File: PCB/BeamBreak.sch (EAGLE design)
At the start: 8 parts, among them J1 AUDIO-CONNECTOR-6P-SMD-344003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, Q1 MOSFET-N-0440200P1

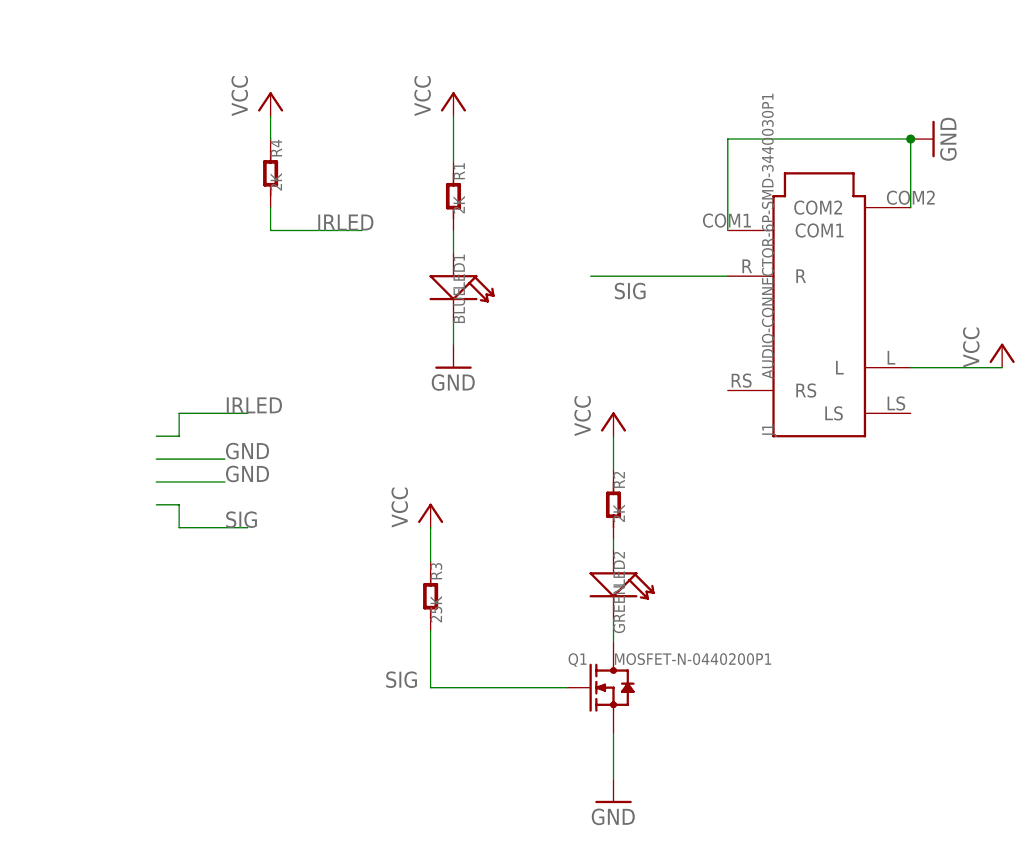
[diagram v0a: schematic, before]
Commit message: Changed connections for wires to a header so that solder mask will be properly applied.
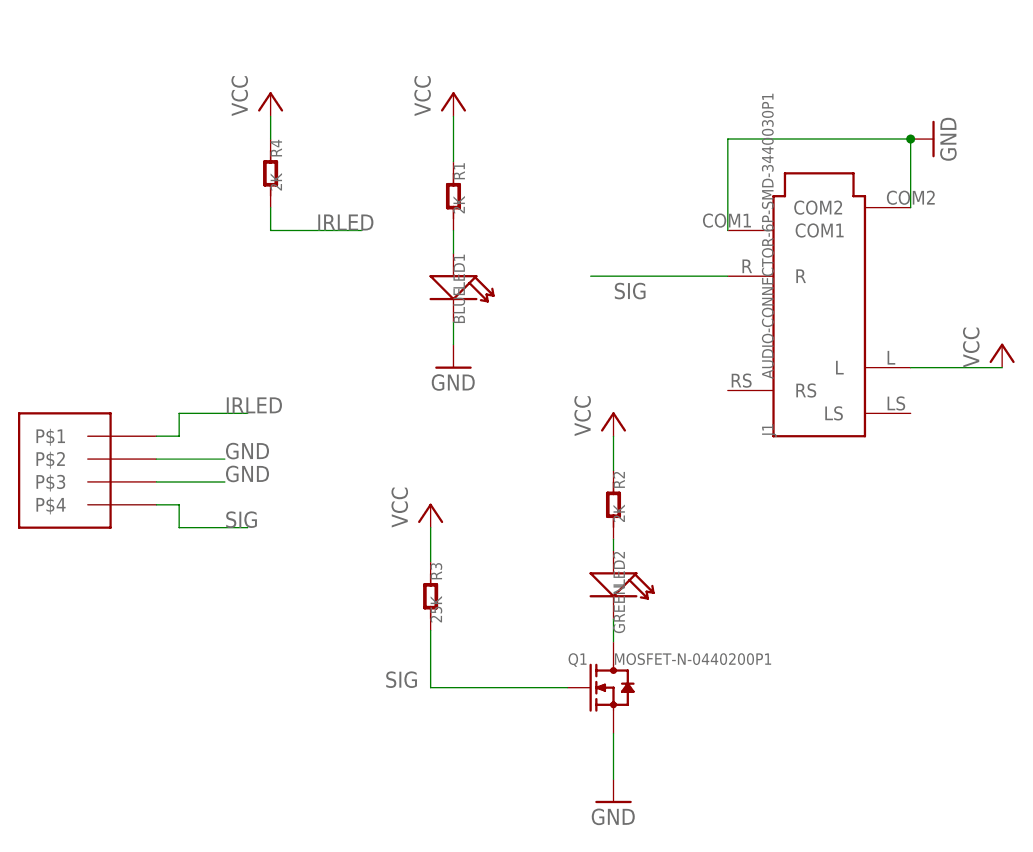
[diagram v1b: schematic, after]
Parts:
- added U$1: HO4, BeamBreak:HO4
- J1: device OPL:AUDIO-CONNECTOR-6P-SMD-3440030P1 -> BeamBreak:AUDIO-CONNECTOR-6P-SMD-3440030P1
- LED1, LED2: device OPL:LED -> BeamBreak:LED
- Q1: device OPL:MOSFET-N-0440200P1 -> BeamBreak:MOSFET-N-0440200P1
- R1, R2, R3: device OPL:R-0603 -> BeamBreak:R-0603
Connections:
- net GND: now also U$1.P$2, U$1.P$3
- net IRLED: now also U$1.P$1
- net SIG: now also U$1.P$4
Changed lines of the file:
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@@
 </classes>
 <parts>
-<part name="R3" library="OPL" deviceset="R*" device="-0603" value="25K"/>
+<part name="R3" library="BeamBreak" deviceset="R*" device="-0603" value="25K"/>
 <part name="GND2" library="SparkFun" deviceset="GND" device=""/>
 <part name="P+3" library="supply1" deviceset="VCC" device=""/>
 <part name="P+4" library="supply1" deviceset="VCC" device=""/>
-<part name="R2" library="OPL" deviceset="R*" device="-0603" value="2K"/>
+<part name="R2" library="BeamBreak" deviceset="R*" device="-0603" value="2K"/>
 <part name="P+5" library="supply1" deviceset="VCC" device=""/>
 <part name="GND5" library="SparkFun" deviceset="GND" device=""/>
-<part name="R1" library="OPL" deviceset="R*" device="-0603" value="2K"/>
+<part name="R1" library="BeamBreak" deviceset="R*" device="-0603" value="2K"/>
 <part name="P+1" library="supply1" deviceset="VCC" device=""/>
-<part name="J1" library="OPL" deviceset="AUDIO-CONNECTOR-6P-SMD" device="-3440030P1"/>
-<part name="LED1" library="OPL" deviceset="LED*" device="" value="BLUE"/>
-<part name="LED2" library="OPL" deviceset="LED*" device="" value="GREEN"/>
+<part name="J1" library="BeamBreak" deviceset="AUDIO-CONNECTOR-6P-SMD" device="-3440030P1"/>
+<part name="LED1" library="BeamBreak" deviceset="LED*" device="" value="BLUE"/>
+<part name="LED2" library="BeamBreak" deviceset="LED*" device="" value="GREEN"/>
 <part name="GND6" library="SparkFun" deviceset="GND" device=""/>
 <part name="P+6" library="supply1" deviceset="VCC" device=""/>
-<part name="Q1" library="OPL" deviceset="MOSFET-N" device="-0440200P1"/>
+<part name="Q1" library="BeamBreak" deviceset="MOSFET-N" device="-0440200P1"/>
 <part name="R4" library="OPL" deviceset="R*" device="-0603" value="2K"/>
+<part name="U$1" library="BeamBreak" deviceset="HO4" device=""/>
 </parts>
 <sheets>
@@
 <instance part="Q1" gate="Q" x="45.72" y="12.7"/>
 <instance part="R4" gate="R" x="7.62" y="69.85" rot="R270"/>
+<instance part="U$1" gate="G$1" x="-12.7" y="35.56"/>
 </instances>
 <busses>
@@
 <wire x1="-5.08" y1="38.1" x2="2.54" y2="38.1" width="0.1524" layer="91"/>
 <label x="2.54" y="38.1" size="1.778" layer="95"/>
+<pinref part="U$1" gate="G$1" pin="P$2"/>
 </segment>
 <segment>
 <wire x1="-5.08" y1="35.56" x2="2.54" y2="35.56" width="0.1524" layer="91"/>
 <label x="2.54" y="35.56" size="1.778" layer="95"/>
+<pinref part="U$1" gate="G$1" pin="P$3"/>
 </segment>
 </net>
@@
 <wire x1="-2.54" y1="30.48" x2="5.08" y2="30.48" width="0.1524" layer="91"/>
 <label x="2.54" y="30.48" size="1.778" layer="95"/>
+<pinref part="U$1" gate="G$1" pin="P$4"/>
 </segment>
 </net>
@@
 <wire x1="-2.54" y1="43.18" x2="5.08" y2="43.18" width="0.1524" layer="91"/>
 <label x="2.54" y="43.18" size="1.778" layer="95"/>
+<pinref part="U$1" gate="G$1" pin="P$1"/>
 </segment>
 </net>
